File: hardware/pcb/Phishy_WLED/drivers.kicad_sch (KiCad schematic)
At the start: 20 parts, among them Q1 2N7002L, Q10 Q_NMOS_Depletion_GDS, Q11 2N7002L, Q12 Q_NMOS_Depletion_GDS, Q2 2N7002L, Q3 Q_NMOS_Depletion_GDS, Q4 Q_NMOS_Depletion_GDS, Q5 2N7002L, Q7 Q_NMOS_Depletion_GDS, Q9 2N7002L

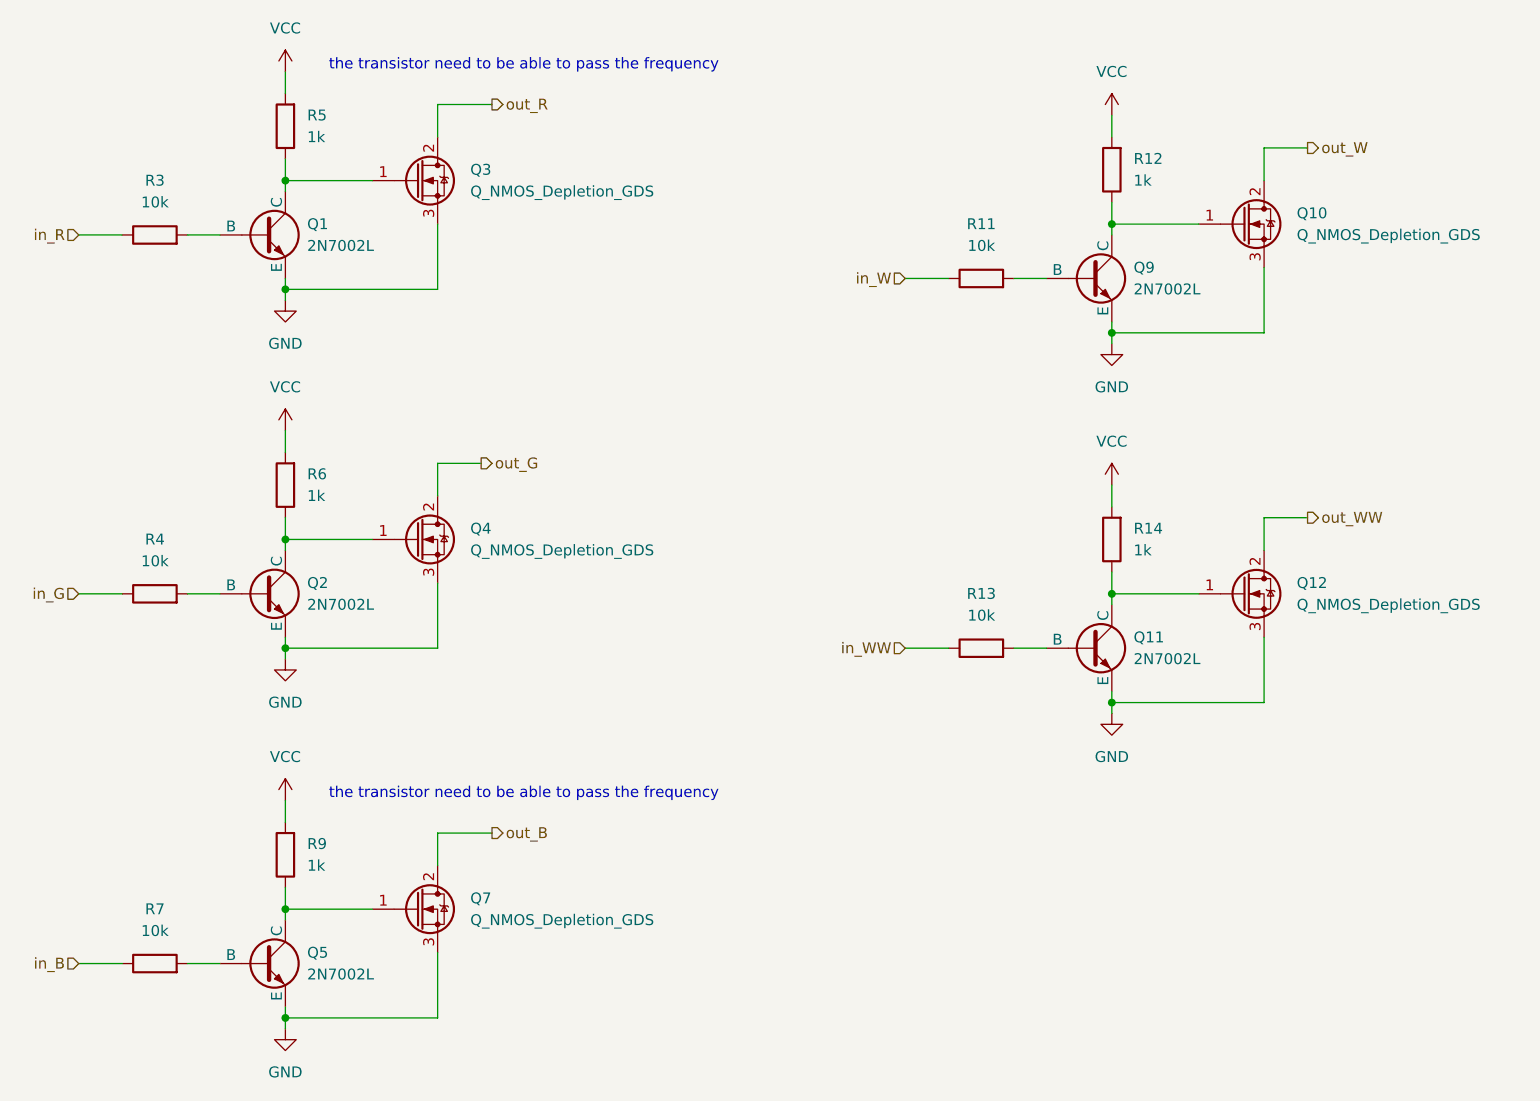
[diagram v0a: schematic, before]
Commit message: footprints added !
all the footprints are here
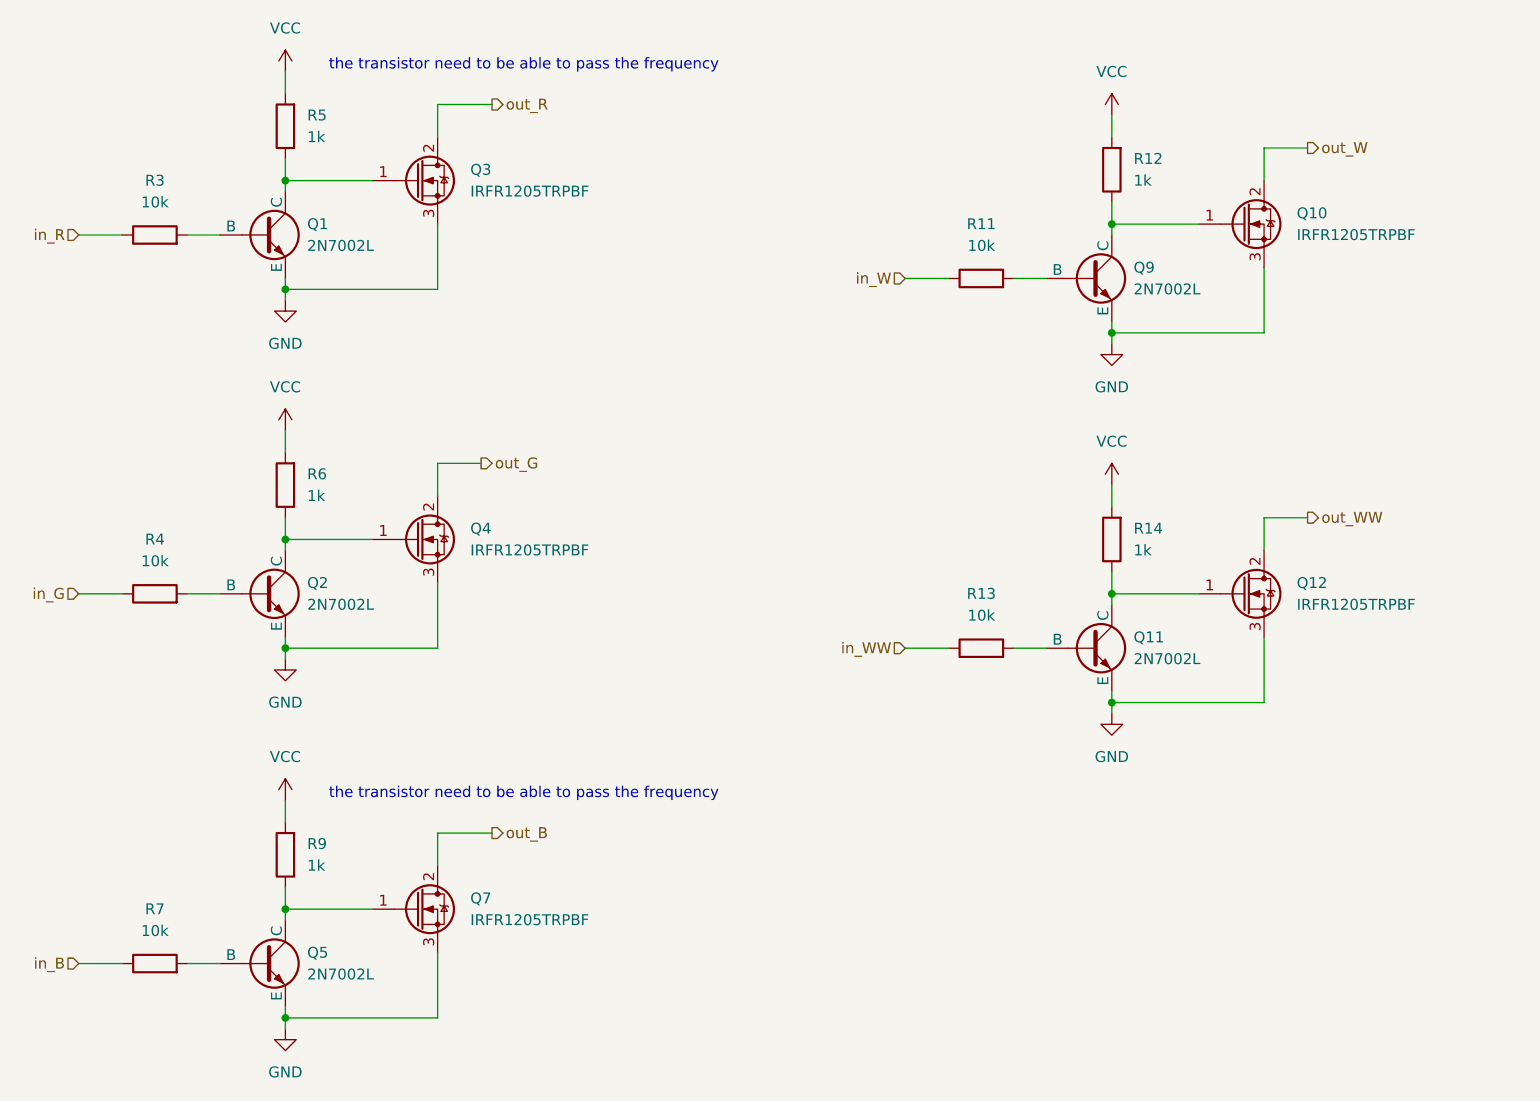
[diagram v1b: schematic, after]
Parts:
- Q10, Q12, Q3, Q4, Q7: value Q_NMOS_Depletion_GDS -> IRFR1205TRPBF; footprint (none) -> Package_TO_SOT_SMD:TO-252-2
- R11, R12, R13, R14, R3, R4, R5, R6, R7, R9: footprint (none) -> Resistor_SMD:R_0603_1608Metric
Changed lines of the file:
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@@
       (effects (font (size 1.27 1.27)) (justify right))
     )
-    (property "Footprint" "" (at 65.278 77.47 90)
+    (property "Footprint" "Resistor_SMD:R_0603_1608Metric" (at 65.278 77.47 90)
       (effects (font (size 1.27 1.27)) hide)
     )
@@
       (effects (font (size 1.27 1.27)))
     )
-    (property "Footprint" "" (at 144.78 98.298 90)
+    (property "Footprint" "Resistor_SMD:R_0603_1608Metric" (at 144.78 98.298 90)
       (effects (font (size 1.27 1.27)) hide)
     )
@@
       (effects (font (size 1.27 1.27)) (justify left))
     )
-    (property "Value" "Q_NMOS_Depletion_GDS" (at 85.09 128.27 0)
-      (effects (font (size 1.27 1.27)) (justify left))
-    )
-    (property "Footprint" "" (at 78.74 127 0)
+    (property "Value" "IRFR1205TRPBF" (at 85.09 128.27 0)
+      (effects (font (size 1.27 1.27)) (justify left))
+    )
+    (property "Footprint" "Package_TO_SOT_SMD:TO-252-2" (at 78.74 127 0)
       (effects (font (size 1.27 1.27)) hide)
     )
@@
       (effects (font (size 1.27 1.27)))
     )
-    (property "Footprint" "" (at 48.26 135.128 90)
+    (property "Footprint" "Resistor_SMD:R_0603_1608Metric" (at 48.26 135.128 90)
       (effects (font (size 1.27 1.27)) hide)
     )
@@
       (effects (font (size 1.27 1.27)))
     )
-    (property "Footprint" "" (at 48.26 91.948 90)
+    (property "Footprint" "Resistor_SMD:R_0603_1608Metric" (at 48.26 91.948 90)
       (effects (font (size 1.27 1.27)) hide)
     )
@@
       (effects (font (size 1.27 1.27)) (justify left))
     )
-    (property "Value" "Q_NMOS_Depletion_GDS" (at 181.61 48.26 0)
-      (effects (font (size 1.27 1.27)) (justify left))
-    )
-    (property "Footprint" "" (at 175.26 46.99 0)
+    (property "Value" "IRFR1205TRPBF" (at 181.61 48.26 0)
+      (effects (font (size 1.27 1.27)) (justify left))
+    )
+    (property "Footprint" "Package_TO_SOT_SMD:TO-252-2" (at 175.26 46.99 0)
       (effects (font (size 1.27 1.27)) hide)
     )
@@
       (effects (font (size 1.27 1.27)))
     )
-    (property "Footprint" "" (at 48.26 50.038 90)
+    (property "Footprint" "Resistor_SMD:R_0603_1608Metric" (at 48.26 50.038 90)
       (effects (font (size 1.27 1.27)) hide)
     )
@@
       (effects (font (size 1.27 1.27)) (justify right))
     )
-    (property "Footprint" "" (at 161.798 40.64 90)
+    (property "Footprint" "Resistor_SMD:R_0603_1608Metric" (at 161.798 40.64 90)
       (effects (font (size 1.27 1.27)) hide)
     )
@@
       (effects (font (size 1.27 1.27)) (justify left))
     )
-    (property "Value" "Q_NMOS_Depletion_GDS" (at 85.09 43.18 0)
-      (effects (font (size 1.27 1.27)) (justify left))
-    )
-    (property "Footprint" "" (at 78.74 41.91 0)
+    (property "Value" "IRFR1205TRPBF" (at 85.09 43.18 0)
+      (effects (font (size 1.27 1.27)) (justify left))
+    )
+    (property "Footprint" "Package_TO_SOT_SMD:TO-252-2" (at 78.74 41.91 0)
       (effects (font (size 1.27 1.27)) hide)
     )
@@
       (effects (font (size 1.27 1.27)))
     )
-    (property "Footprint" "" (at 144.78 55.118 90)
+    (property "Footprint" "Resistor_SMD:R_0603_1608Metric" (at 144.78 55.118 90)
       (effects (font (size 1.27 1.27)) hide)
     )
@@
       (effects (font (size 1.27 1.27)) (justify left))
     )
-    (property "Value" "Q_NMOS_Depletion_GDS" (at 85.09 85.09 0)
-      (effects (font (size 1.27 1.27)) (justify left))
-    )
-    (property "Footprint" "" (at 78.74 83.82 0)
+    (property "Value" "IRFR1205TRPBF" (at 85.09 85.09 0)
+      (effects (font (size 1.27 1.27)) (justify left))
+    )
+    (property "Footprint" "Package_TO_SOT_SMD:TO-252-2" (at 78.74 83.82 0)
       (effects (font (size 1.27 1.27)) hide)
     )
@@
       (effects (font (size 1.27 1.27)) (justify right))
     )
-    (property "Footprint" "" (at 161.798 83.82 90)
+    (property "Footprint" "Resistor_SMD:R_0603_1608Metric" (at 161.798 83.82 90)
       (effects (font (size 1.27 1.27)) hide)
     )
@@
       (effects (font (size 1.27 1.27)) (justify right))
     )
-    (property "Footprint" "" (at 65.278 120.65 90)
+    (property "Footprint" "Resistor_SMD:R_0603_1608Metric" (at 65.278 120.65 90)
       (effects (font (size 1.27 1.27)) hide)
     )
@@
       (effects (font (size 1.27 1.27)) (justify left))
     )
-    (property "Value" "Q_NMOS_Depletion_GDS" (at 181.61 91.44 0)
-      (effects (font (size 1.27 1.27)) (justify left))
-    )
-    (property "Footprint" "" (at 175.26 90.17 0)
+    (property "Value" "IRFR1205TRPBF" (at 181.61 91.44 0)
+      (effects (font (size 1.27 1.27)) (justify left))
+    )
+    (property "Footprint" "Package_TO_SOT_SMD:TO-252-2" (at 175.26 90.17 0)
       (effects (font (size 1.27 1.27)) hide)
     )
@@
       (effects (font (size 1.27 1.27)) (justify right))
     )
-    (property "Footprint" "" (at 65.278 35.56 90)
-      (effects (font (size 1.27 1.27)) hide)
-    )
+    (property "Footprint" "Resistor_SMD:R_0603_1608Metric" (at 65.278 35.56 90)
+      (effects (font (size 1.27 1.27)) hide)
+    )
